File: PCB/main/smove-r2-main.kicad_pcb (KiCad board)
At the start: 4 copper layers, 25 x 30 mm, 53 parts, among them J1 TYPE-C-31-M-12, J2 Battery wire pads 2x 2.54mm, SW1 Off-board pack toggle switch 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, SW2 RESET, SW3 BOOT / USER, U1 ESP32-C3-MINI-1-N4, U2 ICM-20948, U3 PCA9306DCUR, U4 XC6220B331MR-G, U5 AP2112K-1.8TRG1, U6 BQ24074RGTR, U8 USBLC6-2SC6, U9 PESD5V0S2BT,215

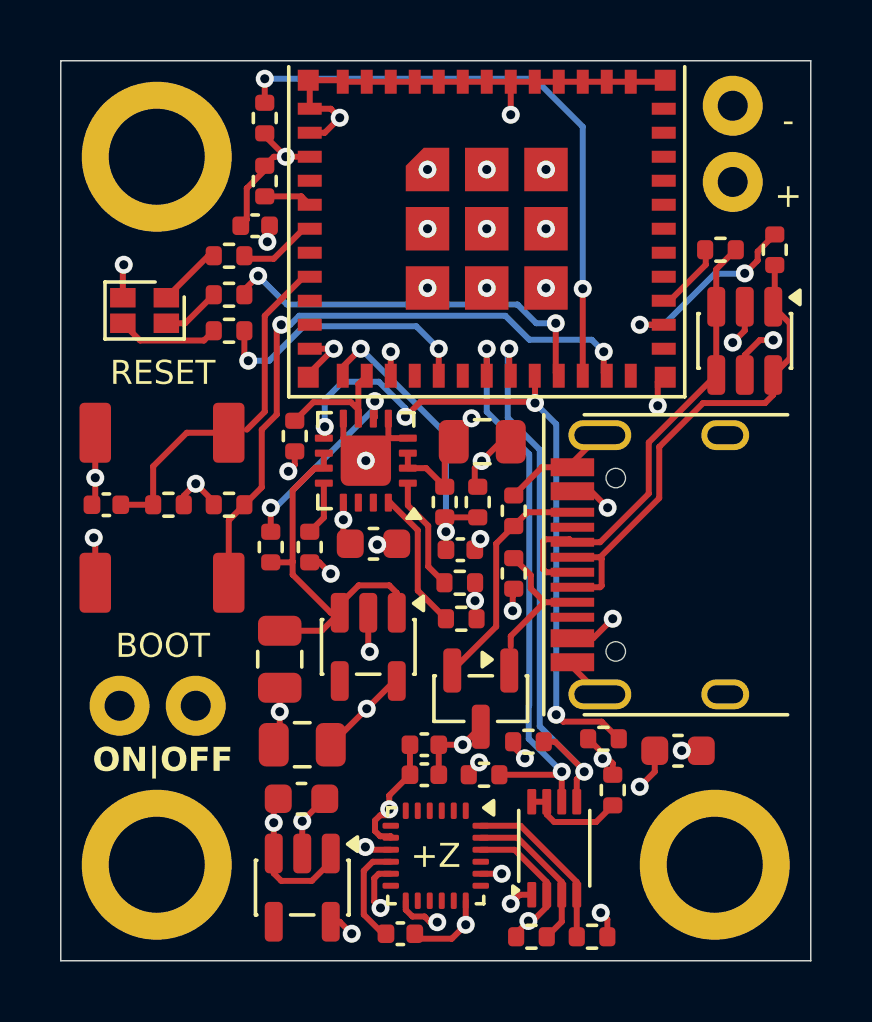
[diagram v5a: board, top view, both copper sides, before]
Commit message: layout: U4 thermal ECO — 8 GND vias + solid GND pours (F.Cu 26.0 mm² / B.Cu 50.0 mm² attached)
- Add 8 × 0.6/0.3 mm GND through vias adjacent to U4's GND pad (no via-in-pad),
  staggered around existing routing; measured min gap to any foreign copper 0.2095 mm.
- Add two solid-connected GND zones U4_THERMAL_F.Cu / U4_THERMAL_B.Cu (priority 1,
  0.2 mm min fill, 0.21 mm clearance) giving 26.008 mm² directly attached copper on
  F.Cu (was 1.058 mm²) and a 50.025 mm² bottom spreader (was 0.212 mm²).
- smove-r2-main.kicad_dru: +6 lines, a 0.21 mm clearance rule scoped to those two
  named zones only (the global 0.15 mm rule overrides zone-local clearance).
- No tracks added/moved/deleted; no footprint, pad, outline or existing-zone change;
  all 570 pre-existing UUID board objects byte-identical; C11's new direct ground
  path hash-verified unchanged.
- Verified: kicad-cli pcb drc (all severities) 0 violations / 0 unconnected; refill
  symmetric difference 0 mm² for all copper zones.
- docs/u4-thermal-eco/: analysis, measurements, DRC reports, reproduction scripts.
- Honest thermal outcome: estimated thetaJA ~250 -> ~236 °C/W (~5.5%), ~6.5 °C lower
  junction at 470 mW — a real but modest improvement; NOT sufficient for sustained
  470-700 mW (projected Tj >150 °C). A lower-loss regulator is the real fix.
- Layout-only: schematics, symbols, footprint libraries and dist/ untouched.
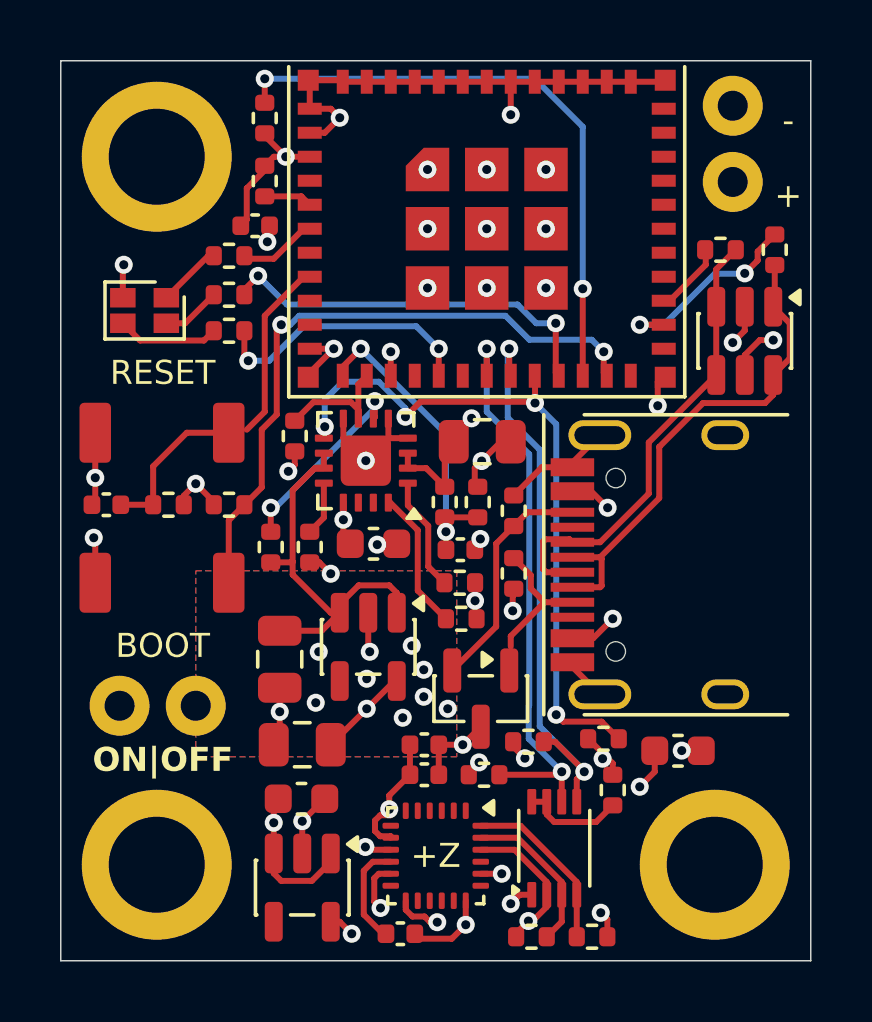
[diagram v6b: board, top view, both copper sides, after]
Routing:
- net GND: vias 35 -> 43
- added copper zone on B.Cu, net GND
- added copper zone on F.Cu, net GND
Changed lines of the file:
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@@
 	)
 	(embedded_fonts no)
+	(via
+		(at 108.5 121.4)
+		(size 0.6)
+		(drill 0.3)
+		(layers "F.Cu" "B.Cu")
+		(net 18)
+	)
+	(via
+		(at 112.1 120.3)
+		(size 0.6)
+		(drill 0.3)
+		(layers "F.Cu" "B.Cu")
+		(net 18)
+	)
+	(via
+		(at 108.6 119.7)
+		(size 0.6)
+		(drill 0.3)
+		(layers "F.Cu" "B.Cu")
+		(net 18)
+	)
+	(via
+		(at 110.2 120.6)
+		(size 0.6)
+		(drill 0.3)
+		(layers "F.Cu" "B.Cu")
+		(net 18)
+	)
+	(via
+		(at 112.1 121.2)
+		(size 0.6)
+		(drill 0.3)
+		(layers "F.Cu" "B.Cu")
+		(net 18)
+	)
+	(via
+		(at 111.4 121.9)
+		(size 0.6)
+		(drill 0.3)
+		(layers "F.Cu" "B.Cu")
+		(net 18)
+	)
+	(via
+		(at 111.7 119.5)
+		(size 0.6)
+		(drill 0.3)
+		(layers "F.Cu" "B.Cu")
+		(net 18)
+	)
+	(via
+		(at 112.9 121.6)
+		(size 0.6)
+		(drill 0.3)
+		(layers "F.Cu" "B.Cu")
+		(net 18)
+	)
+	(zone
+		(net 18)
+		(net_name "GND")
+		(layer "F.Cu")
+		(name "U4_THERMAL_F.Cu")
+		(hatch edge 0.5)
+		(priority 1)
+		(connect_pads yes
+			(clearance 0.21)
+		)
+		(min_thickness 0.2)
+		(filled_areas_thickness no)
+		(fill yes
+			(thermal_gap 0.5)
+			(thermal_bridge_width 0.5)
+		)
+		(polygon
+			(pts
+				(xy 104.5 117) (xy 113.2 117) (xy 113.2 123.2) (xy 104.5 123.2)
+			)
+		)
+	)
+	(zone
+		(net 18)
+		(net_name "GND")
+		(layer "B.Cu")
+		(name "U4_THERMAL_B.Cu")
+		(hatch edge 0.5)
+		(priority 1)
+		(connect_pads yes
+			(clearance 0.21)
+		)
+		(min_thickness 0.2)
+		(filled_areas_thickness no)
+		(fill yes
+			(thermal_gap 0.5)
+			(thermal_bridge_width 0.5)
+		)
+		(polygon
+			(pts
+				(xy 104.5 117) (xy 113.2 117) (xy 113.2 123.2) (xy 104.5 123.2)
+			)
+		)
+	)
 )

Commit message: fab: eliminate JLCPCB export warnings (H1-H3 mounting holes in schematic, U4 footprint aligned)
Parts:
- U4: footprint smove-r2-main:SOT-23-5 -> smove-r2-main:SOT-25_XC6220
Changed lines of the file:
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@@
 		)
 	)
-	(footprint "smove-r2-main:SOT-23-5"
+	(footprint "smove-r2-main:SOT-25_XC6220"
 		(layer "F.Cu")
 		(at 110.25 119.5375 -90)
@@
 			)
 		)
-		(attr through_hole board_only exclude_from_pos_files exclude_from_bom)
+		(sheetname "/Power/")
+		(sheetfile "power.kicad_sch")
+		(attr through_hole exclude_from_pos_files exclude_from_bom)
 		(fp_circle
 			(center 0 0)
@@
 			)
 		)
-		(attr through_hole board_only exclude_from_pos_files exclude_from_bom)
+		(sheetname "/Power/")
+		(sheetfile "power.kicad_sch")
+		(attr through_hole exclude_from_pos_files exclude_from_bom)
 		(fp_circle
 			(center 0 0)
@@
 			)
 		)
-		(attr through_hole board_only exclude_from_pos_files exclude_from_bom)
+		(sheetname "/Power/")
+		(sheetfile "power.kicad_sch")
+		(attr through_hole exclude_from_pos_files exclude_from_bom)
 		(fp_circle
 			(center 0 0)
